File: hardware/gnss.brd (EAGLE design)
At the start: 33.5 x 34.6 mm, 39 parts, among them J1 MICRO_USB_B_HIROSE_ZX62-B-5PA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, SW1 TVAF06-A020B-R, U2 NJM12888F, X1 FA-238

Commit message: 微修正
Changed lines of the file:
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@@
 <wire x1="-2.53" y1="-4.763" x2="-1.57" y2="-4.763" width="0.2" layer="1"/>
 <wire x1="-1.57" y1="-4.763" x2="-0.9235" y2="-5.4095" width="0.2" layer="1"/>
-<wire x1="2.906" y1="-4.064" x2="2.35" y2="-4.064" width="0.2" layer="1"/>
-<wire x1="2.35" y1="-4.064" x2="2.159" y2="-3.873" width="0.2" layer="1"/>
-<via x="2.159" y="-3.873" extent="1-16" drill="0.3"/>
+<wire x1="2.906" y1="-4.064" x2="2.615" y2="-4.064" width="0.2" layer="1"/>
+<wire x1="2.615" y1="-4.064" x2="2.1105" y2="-3.5595" width="0.2" layer="1"/>
+<via x="2.1105" y="-3.5595" extent="1-16" drill="0.3"/>
 <wire x1="-2.53" y1="-2.223" x2="-2.275" y2="-1.968" width="0.2" layer="16"/>
 <wire x1="-2.53" y1="-2.223" x2="-2.53" y2="-4.763" width="0.2" layer="16"/>
@@
 <wire x1="0" y1="-1.968" x2="-0.127" y2="-2.095" width="0.2" layer="16"/>
 <wire x1="-0.127" y1="-2.095" x2="-0.127" y2="-3.683" width="0.2" layer="16"/>
-<wire x1="-0.127" y1="-3.683" x2="0.063" y2="-3.873" width="0.2" layer="16"/>
-<wire x1="0.063" y1="-3.873" x2="2.159" y2="-3.873" width="0.2" layer="16"/>
+<wire x1="-0.127" y1="-3.683" x2="-0.063" y2="-3.747" width="0.2" layer="16"/>
+<wire x1="1.923" y1="-3.747" x2="-0.063" y2="-3.747" width="0.2" layer="16"/>
+<wire x1="1.923" y1="-3.747" x2="2.1105" y2="-3.5595" width="0.2" layer="16"/>
 <wire x1="7.3495" y1="-7.6365" x2="7.3495" y2="-7.003975" width="0.2" layer="1"/>
 <wire x1="7.3495" y1="-7.003975" x2="7.482475" y2="-6.871" width="0.2" layer="1"/>
@@
 <wire x1="7.096" y1="-7.89" x2="7.3495" y2="-7.6365" width="0.2" layer="1"/>
 <contactref element="RP1" pad="26"/>
-<via x="1.778" y="-4.7" extent="1-16" drill="0.3"/>
+<via x="1.841" y="-4.637" extent="1-16" drill="0.3"/>
 <wire x1="1.605475" y1="-4.8318" x2="1.6462" y2="-4.8318" width="0.1524" layer="1"/>
-<wire x1="1.6462" y1="-4.8318" x2="1.778" y2="-4.7" width="0.1524" layer="1"/>
+<wire x1="1.6462" y1="-4.8318" x2="1.841" y2="-4.637" width="0.1524" layer="1"/>
 <wire x1="1.375" y1="-5.455" x2="1.375" y2="-5.062275" width="0.1524" layer="1"/>
 <wire x1="1.375" y1="-5.062275" x2="1.605475" y2="-4.8318" width="0.1524" layer="1"/>
-<wire x1="2.159" y1="-3.873" x2="1.778" y2="-4.254" width="0.1524" layer="16"/>
-<wire x1="1.778" y1="-4.254" x2="1.778" y2="-4.7" width="0.1524" layer="16"/>
+<wire x1="2.1105" y1="-3.5595" x2="1.841" y2="-3.829" width="0.1524" layer="16"/>
+<wire x1="1.841" y1="-3.829" x2="1.841" y2="-4.637" width="0.1524" layer="16"/>
 </signal>
 <signal name="GND">
@@
 <wire x1="-3.19" y1="-4.064" x2="-3.19" y2="-3.988975" width="0.2" layer="1"/>
 <wire x1="-2.588025" y1="-3.387" x2="-3.19" y2="-3.988975" width="0.2" layer="1"/>
-<wire x1="-0.142" y1="-4.064" x2="0.535" y2="-3.387" width="0.2" layer="1"/>
-<wire x1="3.641" y1="-3.387" x2="4.318" y2="-4.064" width="0.2" layer="1"/>
-<wire x1="0.535" y1="-3.387" x2="3.641" y2="-3.387" width="0.2" layer="1"/>
+<wire x1="-0.142" y1="-4.064" x2="0.85" y2="-3.072" width="0.2" layer="1"/>
+<wire x1="3.326" y1="-3.072" x2="4.318" y2="-4.064" width="0.2" layer="1"/>
+<wire x1="0.85" y1="-3.072" x2="3.326" y2="-3.072" width="0.2" layer="1"/>
 <wire x1="4.175" y1="-5.455" x2="4.175" y2="-6.223" width="0.2" layer="1"/>
 <wire x1="4.175" y1="-6.223" x2="4.175" y2="-7.89" width="0.2" layer="1"/>
@@
 <wire x1="-0.415" y1="1.366" x2="-0.415" y2="3.395" width="0.1524" layer="1"/>
 <polygon width="0.1524" layer="16">
-<vertex x="-19.558" y="21.971"/>
+<vertex x="-19.558" y="19.812"/>
 <vertex x="-19.558" y="-18.034"/>
 <vertex x="-18.923" y="-18.669"/>
@@
 <vertex x="18.288" y="19.431"/>
 <vertex x="17.907" y="19.812"/>
-<vertex x="-19.558" y="19.812"/>
-<vertex x="-20.066" y="19.304"/>
 </polygon>
-<wire x1="11.811" y1="12.7" x2="14.097" y2="10.16" width="0" layer="19" extent="1-1"/>
-<wire x1="16.002" y1="6.985" x2="14.097" y2="10.16" width="0" layer="19" extent="1-1"/>
-<wire x1="15.5" y1="5.08" x2="16.002" y2="6.985" width="0" layer="19" extent="1-1"/>
-<wire x1="16.256" y1="3.81" x2="15.5" y2="5.08" width="0" layer="19" extent="1-1"/>
-<wire x1="13.8385" y1="5.0585" x2="15.5" y2="5.08" width="0" layer="19" extent="1-1"/>
-<wire x1="14.605" y1="1.27" x2="14.605" y2="3.556" width="0" layer="19" extent="1-1"/>
-<wire x1="13.171" y1="1.511" x2="14.605" y2="1.27" width="0" layer="19" extent="1-1"/>
-<wire x1="16.256" y1="1.27" x2="14.605" y2="1.27" width="0" layer="19" extent="1-1"/>
-<wire x1="13.589" y1="-1.016" x2="14.605" y2="1.27" width="0" layer="19" extent="1-1"/>
-<wire x1="16.256" y1="-1.27" x2="16.256" y2="1.27" width="0" layer="19" extent="1-1"/>
-<wire x1="16.256" y1="-3.81" x2="16.256" y2="-1.27" width="0" layer="19" extent="1-1"/>
-<wire x1="6.3165" y1="-15.241" x2="6.35" y2="-15.255" width="0" layer="19" extent="1-1"/>
-<wire x1="-1.27" y1="-15.255" x2="-1.2" y2="-15.24" width="0" layer="19" extent="1-16"/>
-<wire x1="-3.49" y1="-12.6605" x2="-3.1" y2="-12.69" width="0" layer="19" extent="16-16"/>
-<wire x1="0.635" y1="-15.24" x2="1.2" y2="-15.24" width="0" layer="19" extent="16-16"/>
-<wire x1="10.541" y1="-6.35" x2="9.667" y2="-6.35" width="0" layer="19" extent="1-1"/>
-<wire x1="5.954" y1="-4.064" x2="5.08" y2="-4.064" width="0" layer="19" extent="1-1"/>
-<wire x1="-1.071" y1="-3.906" x2="-0.142" y2="-4.064" width="0" layer="19" extent="1-1"/>
-<wire x1="1.185" y1="-1.714" x2="-0.015" y2="-1.714" width="0" layer="19" extent="1-1"/>
-<wire x1="16.256" y1="-6.35" x2="15.5" y2="-5.08" width="0" layer="19" extent="1-1"/>
-<wire x1="-16.129" y1="-6.604" x2="-15.5" y2="-5.08" width="0" layer="19" extent="1-1"/>
-<wire x1="14.605" y1="-3.683" x2="16.256" y2="-3.81" width="0" layer="19" extent="1-1"/>
-<wire x1="9.779" y1="-4.445" x2="9.667" y2="-6.35" width="0" layer="19" extent="1-1"/>
-<wire x1="11.811" y1="-9.652" x2="13.589" y2="-10.414" width="0" layer="19" extent="1-1"/>
-<wire x1="-10.287" y1="-8.128" x2="-8.89" y2="-6.665" width="0" layer="19" extent="1-1"/>
-<wire x1="-11.303" y1="-7.366" x2="-10.287" y2="-8.128" width="0" layer="19" extent="1-1"/>
-<wire x1="-11.592" y1="-5.985" x2="-11.303" y2="-7.366" width="0" layer="19" extent="1-1"/>
-<wire x1="-11.4345" y1="-4.6935" x2="-11.592" y2="-5.985" width="0" layer="19" extent="1-1"/>
-<wire x1="-13.45" y1="-4.0235" x2="-11.4345" y2="-4.6935" width="0" layer="19" extent="1-1"/>
-<wire x1="-13.462" y1="-1.905" x2="-13.45" y2="-4.0235" width="0" layer="19" extent="1-1"/>
-<wire x1="-6.8895" y1="-4.8605" x2="-4.938" y2="-4.064" width="0" layer="19" extent="1-1"/>
-<wire x1="12.573" y1="-4.318" x2="14.605" y2="-3.683" width="0" layer="19" extent="1-1"/>
-<wire x1="-8.886" y1="-10.1735" x2="-7.0195" y2="-8.89" width="0" layer="19" extent="1-1"/>
-<wire x1="-13.843" y1="-7.239" x2="-16.129" y2="-6.604" width="0" layer="19" extent="1-1"/>
-<wire x1="-14.732" y1="-9.144" x2="-13.843" y2="-7.239" width="0" layer="19" extent="1-1"/>
-<wire x1="-9.3035" y1="-3.6485" x2="-11.4345" y2="-4.6935" width="0" layer="19" extent="1-1"/>
-<wire x1="-12.065" y1="-9.779" x2="-10.287" y2="-8.128" width="0" layer="19" extent="1-1"/>
-<wire x1="-13.081" y1="-11.43" x2="-12.065" y2="-9.779" width="0" layer="19" extent="1-1"/>
-<wire x1="12.954" y1="-6.985" x2="10.541" y2="-6.35" width="0" layer="19" extent="1-1"/>
-<wire x1="-16.256" y1="-1.27" x2="-16.256" y2="-3.81" width="0" layer="19" extent="1-1"/>
-<wire x1="-16.256" y1="1.27" x2="-16.256" y2="-1.27" width="0" layer="19" extent="1-1"/>
-<wire x1="-14.605" y1="1.27" x2="-16.256" y2="1.27" width="0" layer="19" extent="1-1"/>
-<wire x1="-14.097" y1="2.286" x2="-14.605" y2="1.27" width="0" layer="19" extent="1-1"/>
-<wire x1="-14.605" y1="3.81" x2="-14.097" y2="2.286" width="0" layer="19" extent="1-1"/>
-<wire x1="-15.5" y1="5.08" x2="-14.605" y2="3.81" width="0" layer="19" extent="1-1"/>
-<wire x1="-3.81" y1="17.018" x2="-3.725" y2="15.736" width="0" layer="19" extent="1-1"/>
-<wire x1="1.27" y1="17.399" x2="3.06" y2="16.51" width="0" layer="19" extent="1-1"/>
-<wire x1="-1.27" y1="17.399" x2="1.27" y2="17.399" width="0" layer="19" extent="1-1"/>
-<wire x1="-15.621" y1="7.62" x2="-15.5" y2="5.08" width="0" layer="19" extent="1-1"/>
-<wire x1="-6.35" y1="16.256" x2="-3.81" y2="17.018" width="0" layer="19" extent="1-1"/>
-<wire x1="-14.097" y1="10.16" x2="-15.621" y2="7.62" width="0" layer="19" extent="1-1"/>
-<wire x1="8.89" y1="14.986" x2="11.811" y2="12.7" width="0" layer="19" extent="1-1"/>
-<wire x1="-11.43" y1="13.081" x2="-14.097" y2="10.16" width="0" layer="19" extent="1-1"/>
 </signal>
 <signal name="USB_DM">
@@
 <wire x1="2.575" y1="-6.823" x2="2.575" y2="-5.455" width="0.2" layer="1"/>
 <wire x1="0.4125" y1="-10.8265" x2="0.4125" y2="-7.3345" width="0.2" layer="1"/>
-<wire x1="1.158" y1="-4.064" x2="1.779" y2="-4.064" width="0.2" layer="1"/>
-<wire x1="2.575" y1="-4.86" x2="2.575" y2="-5.455" width="0.2" layer="1"/>
-<wire x1="1.779" y1="-4.064" x2="2.575" y2="-4.86" width="0.2" layer="1"/>
+<wire x1="2.0775" y1="-4.064" x2="2.329" y2="-4.3155" width="0.2" layer="1"/>
+<wire x1="2.329" y1="-4.3155" x2="2.329" y2="-4.608025" width="0.2" layer="1"/>
+<wire x1="2.329" y1="-4.608025" x2="2.575" y2="-4.854025" width="0.2" layer="1"/>
+<wire x1="1.158" y1="-4.064" x2="2.0775" y2="-4.064" width="0.2" layer="1"/>
+<wire x1="2.575" y1="-4.854025" x2="2.575" y2="-5.455" width="0.2" layer="1"/>
 </signal>
 <signal name="N$6">

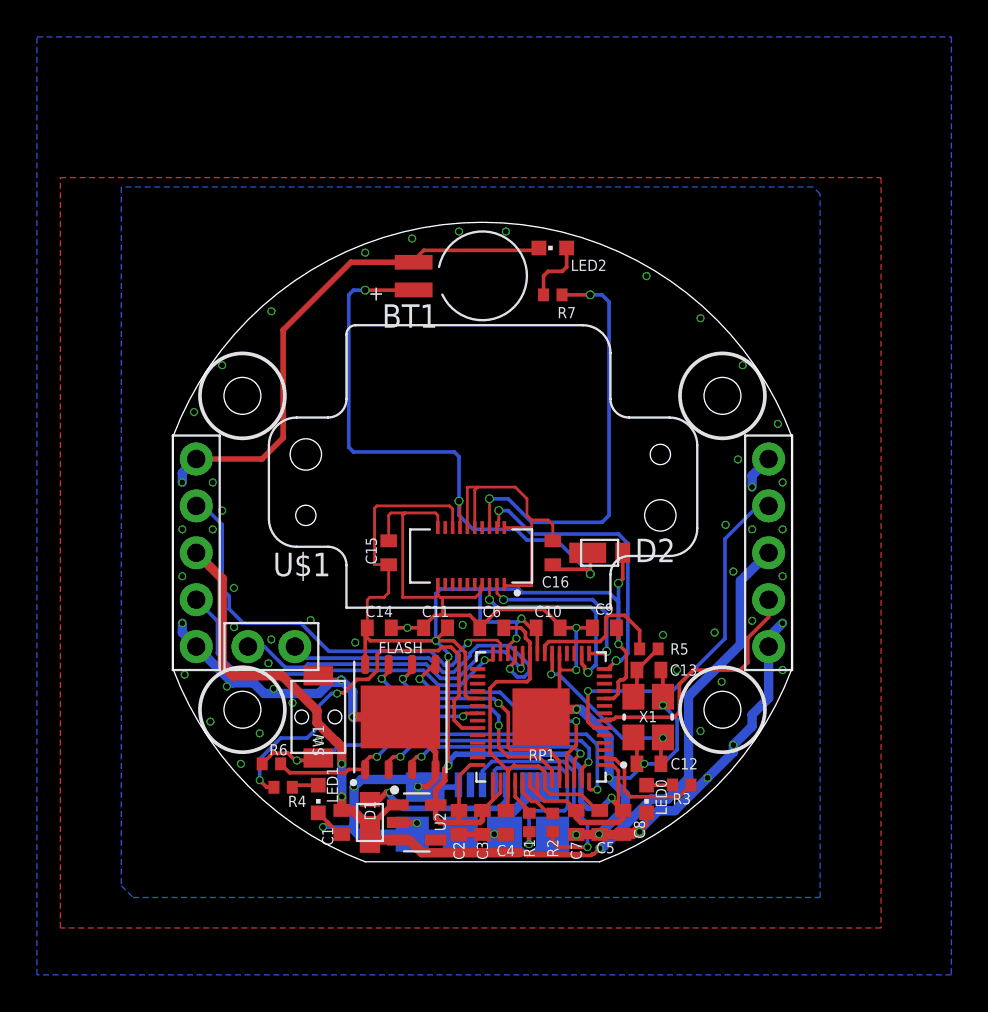
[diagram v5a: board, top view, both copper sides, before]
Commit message: シルクを調整
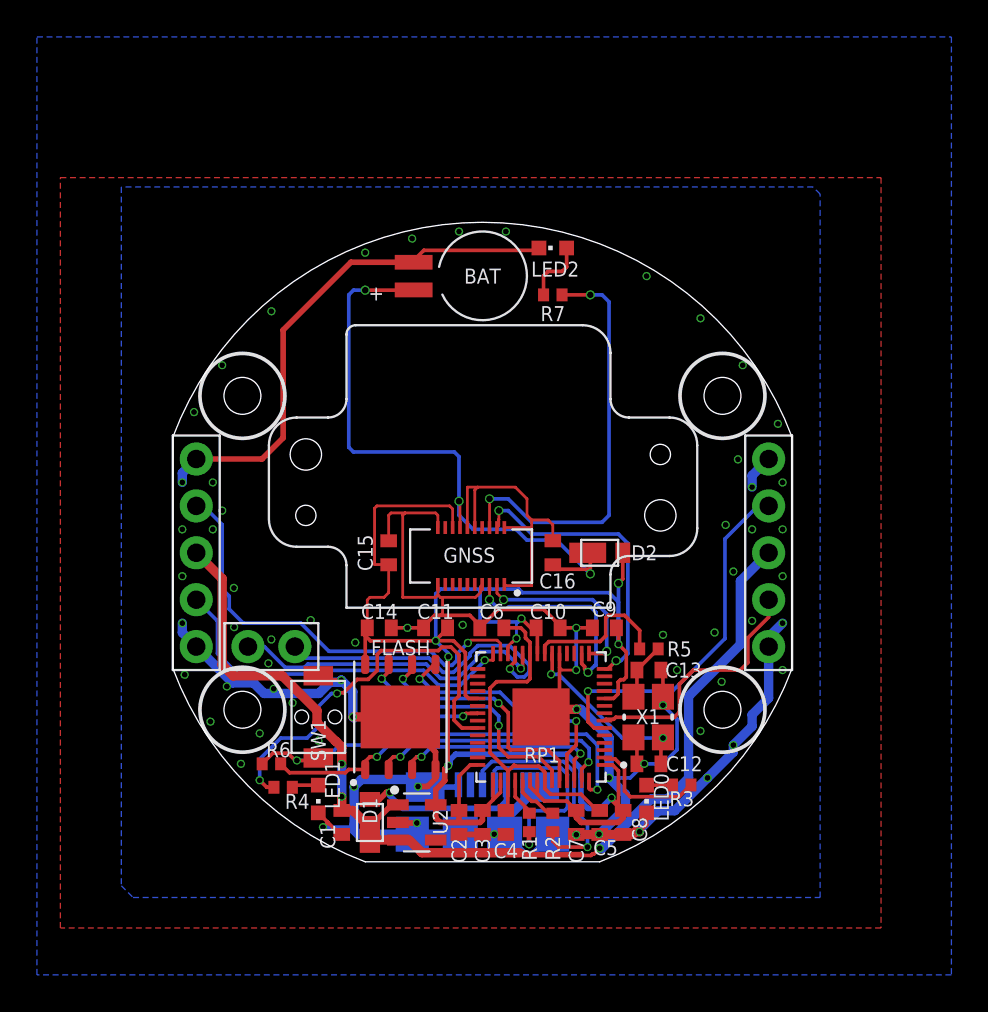
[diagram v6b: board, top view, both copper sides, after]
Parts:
- renumbered BT1 to BAT, U$1 to GNSS
